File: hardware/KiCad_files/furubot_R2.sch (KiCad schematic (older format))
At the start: 74 parts, among them IC1 ULN2803, U1 CONN_01X04, U2 ESP01, U3 CONN_01X04, U4 CONN_01X04, U5 CONN_01X04, U6 LM1117-SOT, X1 Screw_Terminal_1x02

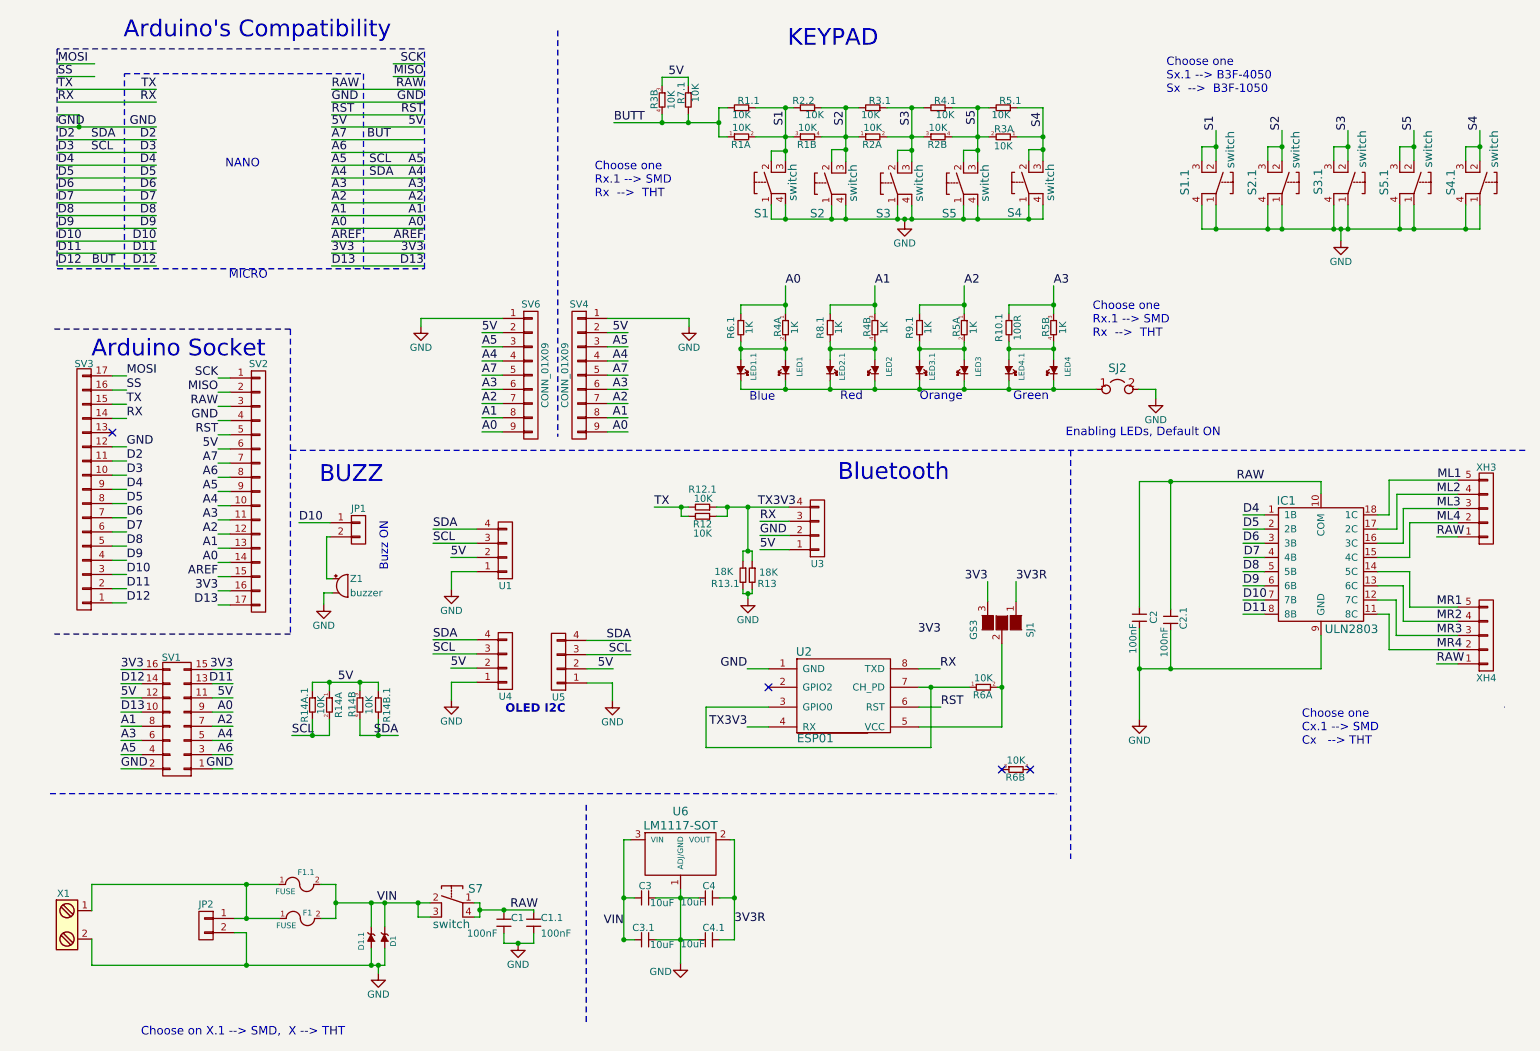
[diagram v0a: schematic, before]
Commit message: Actualización del fichero de layout con las cotas de los drills para la fijacion
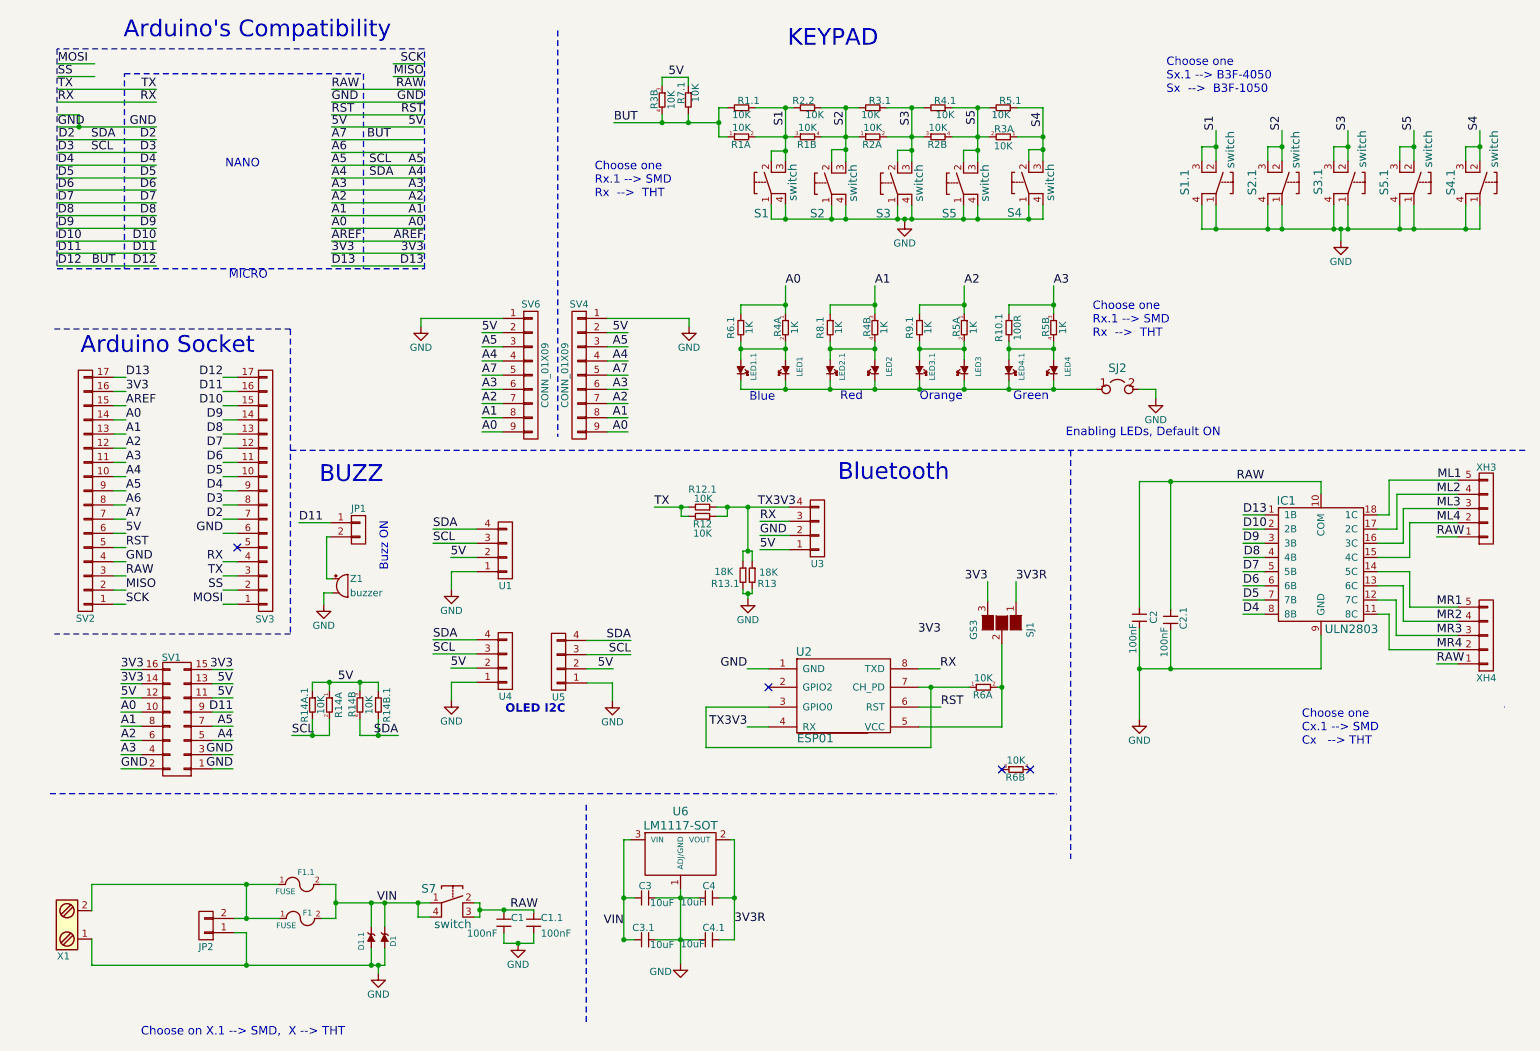
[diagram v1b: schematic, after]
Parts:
- S1, S2, S3, S4, S5: footprint Switch:bf4050_Button -> Switch:Button
- SJ2: footprint Resistors_SMD:R_0402 -> Connect:GS2
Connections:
- net BUTT is gone; now on net A7: R1.1, R1.1.2, R3.4, R7.1.2
- net 3V3: now also SV1.14 (P14)
- net 5V: now also SV1.13 (P13)
- net A0: now also SV1.10 (P10); no longer SV1.9 (P9)
- net A2: now also SV1.6 (P6); no longer SV1.7 (P7)
- net A3: now also SV1.4 (P4); no longer SV1.6 (P6)
- net A4: now also SV3.7 (P7); no longer SV3.11 (P11)
- net A5: now also SV1.7 (P7), SV3.8 (P8); no longer SV1.4 (P4), SV3.10 (P10)
- net A6: no longer SV1.3 (P3)
- net A7: now also SV3.17 (P17); no longer SV1.14 (P14), SV3.1 (P1)
- net D10: now also IC1.2 (2B), SV3.15 (P15); no longer IC1.7 (7B), JP1.1 (P1), SV3.3 (P3)
- net D11: now also JP1.1 (P1), SV1.9 (P9), SV3.16 (P16); no longer IC1.8 (8B), SV1.13 (P13), SV3.2 (P2)
- net D13: now also IC1.1 (1B); no longer SV1.10 (P10)
- net D4: now also IC1.8 (8B); no longer IC1.1 (1B)
- net D5: now also IC1.7 (7B), SV3.10 (P10); no longer IC1.2 (2B), SV3.8 (P8)
- net D6: now also IC1.6 (6B), SV3.11 (P11); no longer IC1.3 (3B), SV3.7 (P7)
- net D7: now also IC1.5 (5B), SV3.12 (P12); no longer IC1.4 (4B), SV3.6 (P6)
- net D8: now also IC1.4 (4B), SV3.13 (P13); no longer IC1.5 (5B), SV3.5 (P5)
- net D9: now also IC1.3 (3B), SV3.14 (P14); no longer IC1.6 (6B), SV3.4 (P4)
- net GND: now also JP2.1 (P1), SV1.3 (P3), SV3.6 (P6), X1.1; no longer JP2.2 (P2), SV3.12 (P12), X1.2
- net MOSI: now also SV3.1 (P1); no longer SV3.17 (P17)
- net RAW: now also S7.2, S7.3; no longer S7.1, S7.4
- net RX: now also SV3.4 (P4); no longer SV3.14 (P14)
- net SS: now also SV3.2 (P2); no longer SV3.16 (P16)
- net TX: now also SV3.3 (P3); no longer SV3.15 (P15)
- net VIN: now also S7.1, S7.4; no longer S7.2, S7.3
- net at F1.1, F1.1.1: now also JP2.2 (P2), X1.2; no longer JP2.1 (P1), X1.1
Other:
- moved on the sheet: SV2, SV3
